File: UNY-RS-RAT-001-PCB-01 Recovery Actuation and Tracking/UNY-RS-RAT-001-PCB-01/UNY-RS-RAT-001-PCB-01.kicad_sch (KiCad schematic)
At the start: 0 parts

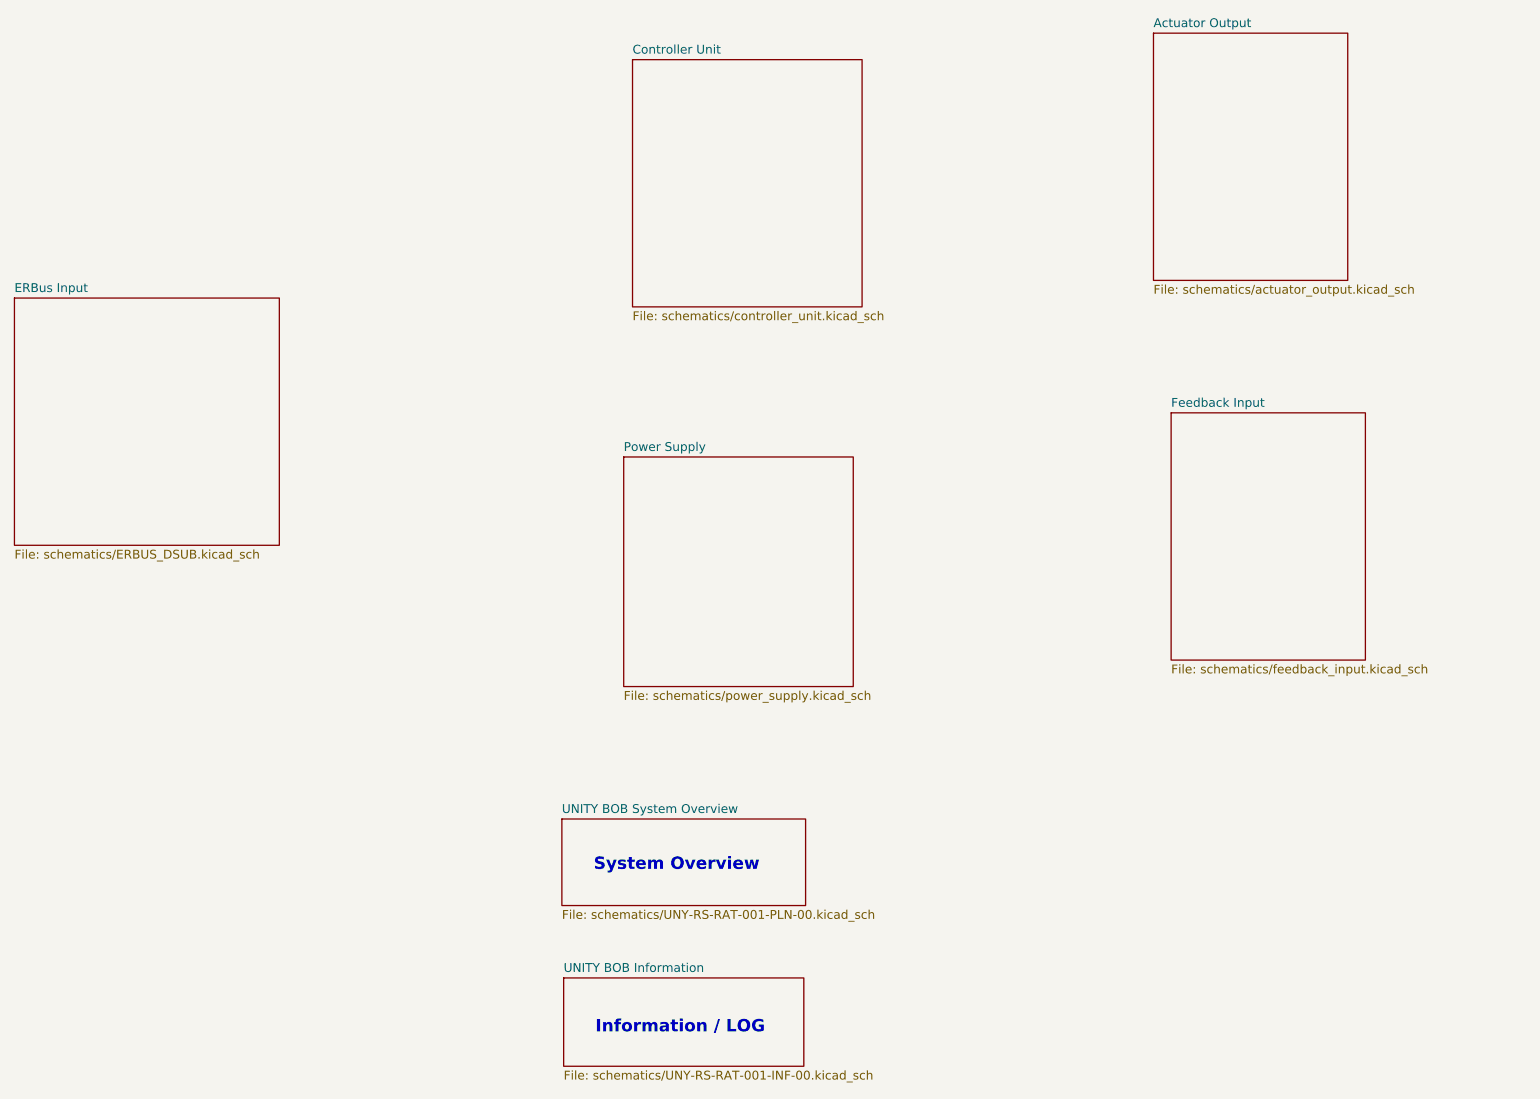
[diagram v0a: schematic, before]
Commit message: First draft for ERBUS, Power & CPU
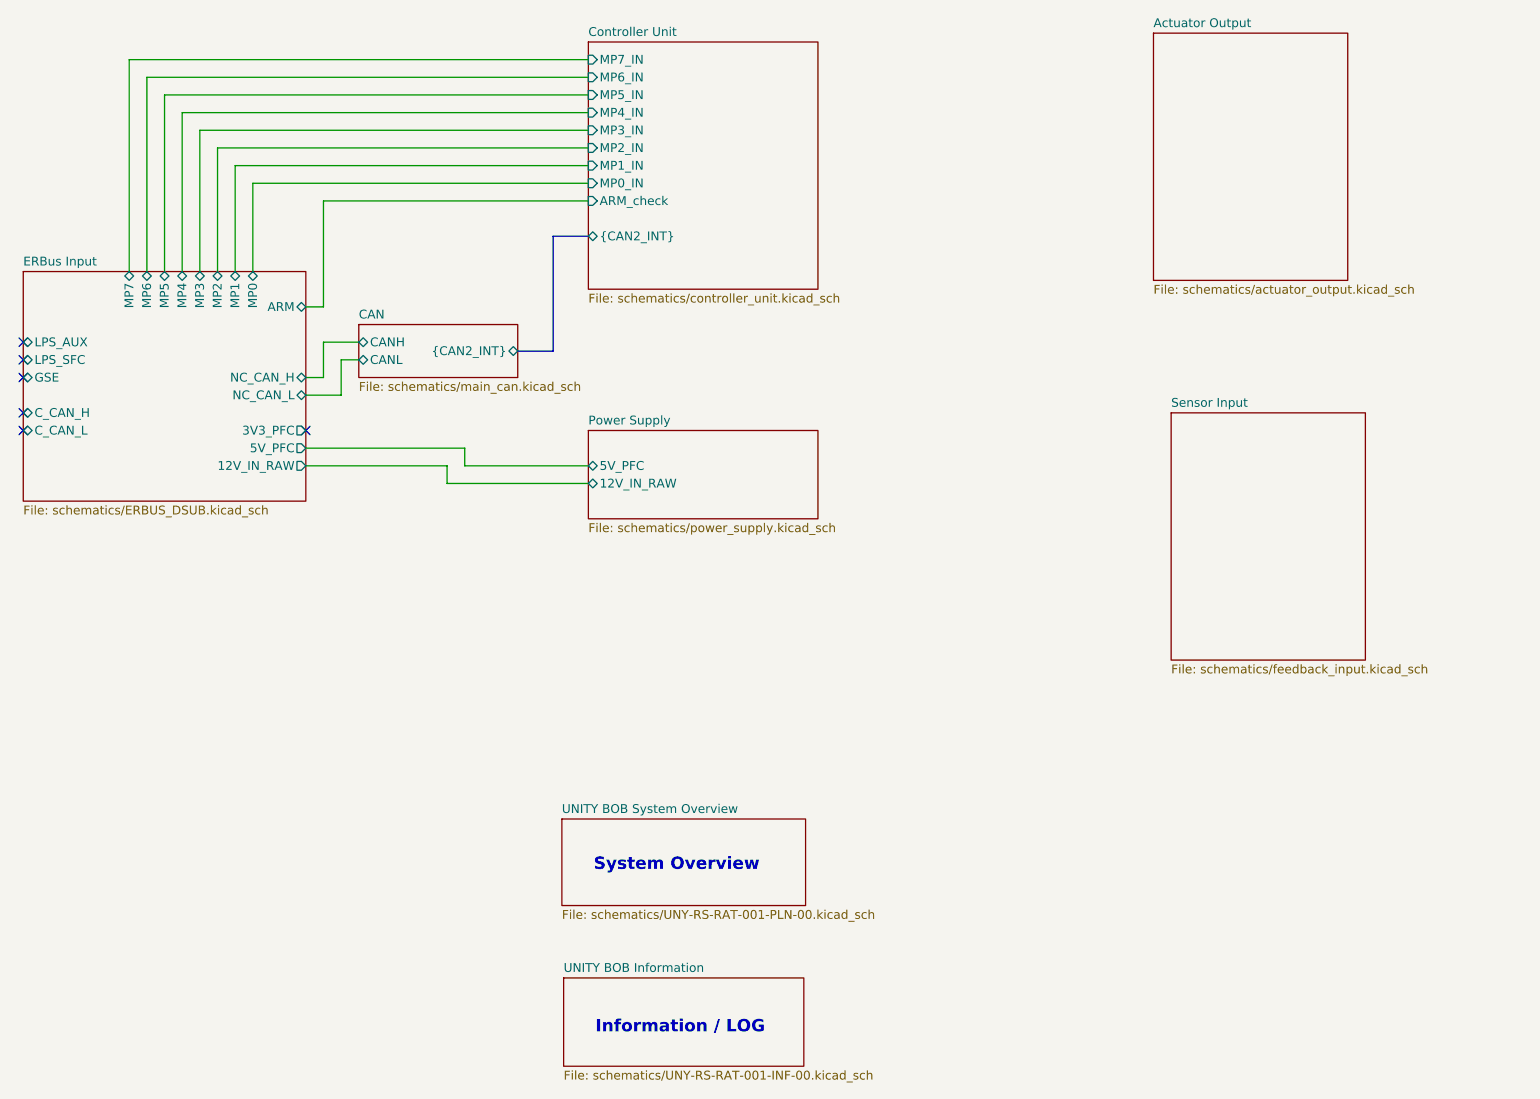
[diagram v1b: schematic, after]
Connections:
- no-connect marks 0 -> 6
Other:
- sheet Feedback Input renamed Sensor Input
- added sheet CAN (schematics/main_can.kicad_sch)
- sheet Controller Unit ports: added ARM_check, MP0_IN, MP1_IN, MP2_IN, MP3_IN, MP4_IN, MP5_IN, MP6_IN, MP7_IN, {CAN2_INT}; removed none
- sheet ERBus Input ports: added 12V_IN_RAW, 3V3_PFC, 5V_PFC, ARM, C_CAN_H, C_CAN_L, GSE, LPS_AUX, LPS_SFC, MP0, MP1, MP2, MP3, MP4, MP5, MP6, MP7, NC_CAN_H, NC_CAN_L; removed none
- sheet Power Supply ports: added 12V_IN_RAW, 5V_PFC; removed none
- title: RAT High level schematics -> Sensor MCU

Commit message: Semi complete, missing footprints and connectors
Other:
- sheet Actuator Output ports: added {PWM_BUS}; removed none
- sheet Controller Unit ports: added {ERBUS_SIG}, {PWM_BUS}, {SPI_Fsense}, {SPI_Psense}; removed ARM_check, MP0_IN, MP1_IN, MP2_IN, MP3_IN, MP4_IN, MP5_IN, MP6_IN, MP7_IN
- sheet Sensor Input ports: added {SPI_Fsense}, {SPI_Psense}; removed none
- company: (none) -> E.R.I.G. e.V
